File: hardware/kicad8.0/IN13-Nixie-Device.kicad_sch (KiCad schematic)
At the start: 35 parts, among them J1 PINHD_1x3_Female, J2 AudioJack3, J3 PINHD_1x4_Male, J4 USB_C_Receptacle_USB2.0_16P, Q2 MMBTA42, T1 Transformer_1P_1S, U1 LM358, U2 STI3508, U3 LD1117S33TR_SOT223, U4 ESP32-C6-MINI-1/U

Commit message: layout progress, kicad proj rename
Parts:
- removed C1: 1uF 16V, Capacitor_SMD:C_0805_2012Metric, symbol PCM_SL_Devices:Capacitor_NP
- removed C2: 10uF 16V, Capacitor_SMD:C_0805_2012Metric, symbol PCM_SL_Devices:Capacitor_NP
- removed D2: D_Schottky, Diode_SMD:D_0805_2012Metric, symbol Device:D_Schottky
- removed U3: LD1117S33TR_SOT223, Package_TO_SOT_THT:TO-220-3_Horizontal_TabDown, symbol Regulator_Linear:LD1117S33TR_SOT223
- added U3: AMS1117-3.3, Package_TO_SOT_SMD:SOT-223-3_TabPin2, symbol Regulator_Linear:AMS1117-3.3
- C10, C11: footprint Capacitor_SMD:C_0805_2012Metric -> Capacitor_SMD:C_0603_1608Metric
- R3, R6, R7, R8: footprint Resistor_SMD:R_0805_2012Metric -> Resistor_SMD:R_0603_1608Metric
- T1: footprint IN13-Device:EE0504S -> IN13-Nixie-Device:EE0504S; symbol IN13-Device:EE0504S_Transformer -> IN13-Nixie-Device:EE0504S_Transformer
- U2: symbol IN13-Device:STI3508 -> IN13-Nixie-Device:STI3508
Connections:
- net +3.3V: no longer T1.4 (AA), U2.5 (VIN)
- net +3V3: now also T1.4 (AA), U2.5 (VIN), U3.2 (VO)
- net GND: now also U3.1 (GND)
- net VBUS: now also C5.1, C6.1, U3.3 (VI)
- net VIN: no longer C5.1, C6.1
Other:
- note added: "Power/HV Boost"
- note removed: "Power"
- moved on the sheet: C3, C5, C6, C7, C8, C9, D1, J2, J3, J4, R1, R10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

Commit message: starting traces
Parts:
- added J5: PINHD_1x4_Male, SharedCustom:Pads_1x4_2.54mm, symbol PCM_SL_Pin_Headers:PINHD_1x4_Male
- added R11: 10k, Resistor_SMD:R_0603_1608Metric, symbol Device:R
- added SW1, SW3: SW_Push, IN13-Nixie-Device:Mitsumi_SOFSeries_SMD_Button, symbol IN13-Nixie-Device:SW_SPST_W_Ground_Pin
- C3: value 220nF 200V -> 0.22u 200V
- J3: footprint Connector_PinHeader_2.54mm:PinHeader_1x04_P2.54mm_Vertical -> SharedCustom:Pads_1x4_2.54mm
- U1: footprint Package_SO:SOIC-8-1EP_3.9x4.9mm_P1.27mm_EP2.41x3.81mm -> Package_SO:SOIC-8_3.9x4.9mm_P1.27mm
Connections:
- net +3V3 is gone; now on net +3.3V: C7.1, C8.1, C9.1, T1.4 (AA), U2.5 (VIN), U3.2 (VO)
- net +3.3V: now also R11.1
- net BOOT: now also SW3.1 (A)
- net GND: now also SW1.2 (B), SW1.3 (GND), SW3.2 (B), SW3.3 (GND)
- net SIGNAL: now also R11.2
- net TDI: now reaches U4.10 (MTDI/GPIO5/ADC1_CH5)
- net TDI: now also J5.2
- net TCK: now reaches U4.15 (MTCK/GPIO6/ADC1_CH6)
- net TCK: now also J5.3
- net TDO: now reaches U4.16 (MTDO/GPIO7)
- net TDO: now also J5.4
- net EN: now reaches C10.1, R6.2, U4.8 (EN/CHIP_PU)
- net EN: now also SW1.1 (A)
- net TMS: now reaches U4.9 (MTMS/GPIO4/ADC1_CH4)
- net TMS: now also J5.1
- no-connect marks 18 -> 14
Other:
- note added: "HV Boost"
- note added: "Power"
- note removed: "Power/HV Boost"
- title: IN-13 Device -> IN-13 Nixie Device
- moved on the sheet: C10, C11, C3, C5, C6, C7, C8, C9, D1, J2, J3, J4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

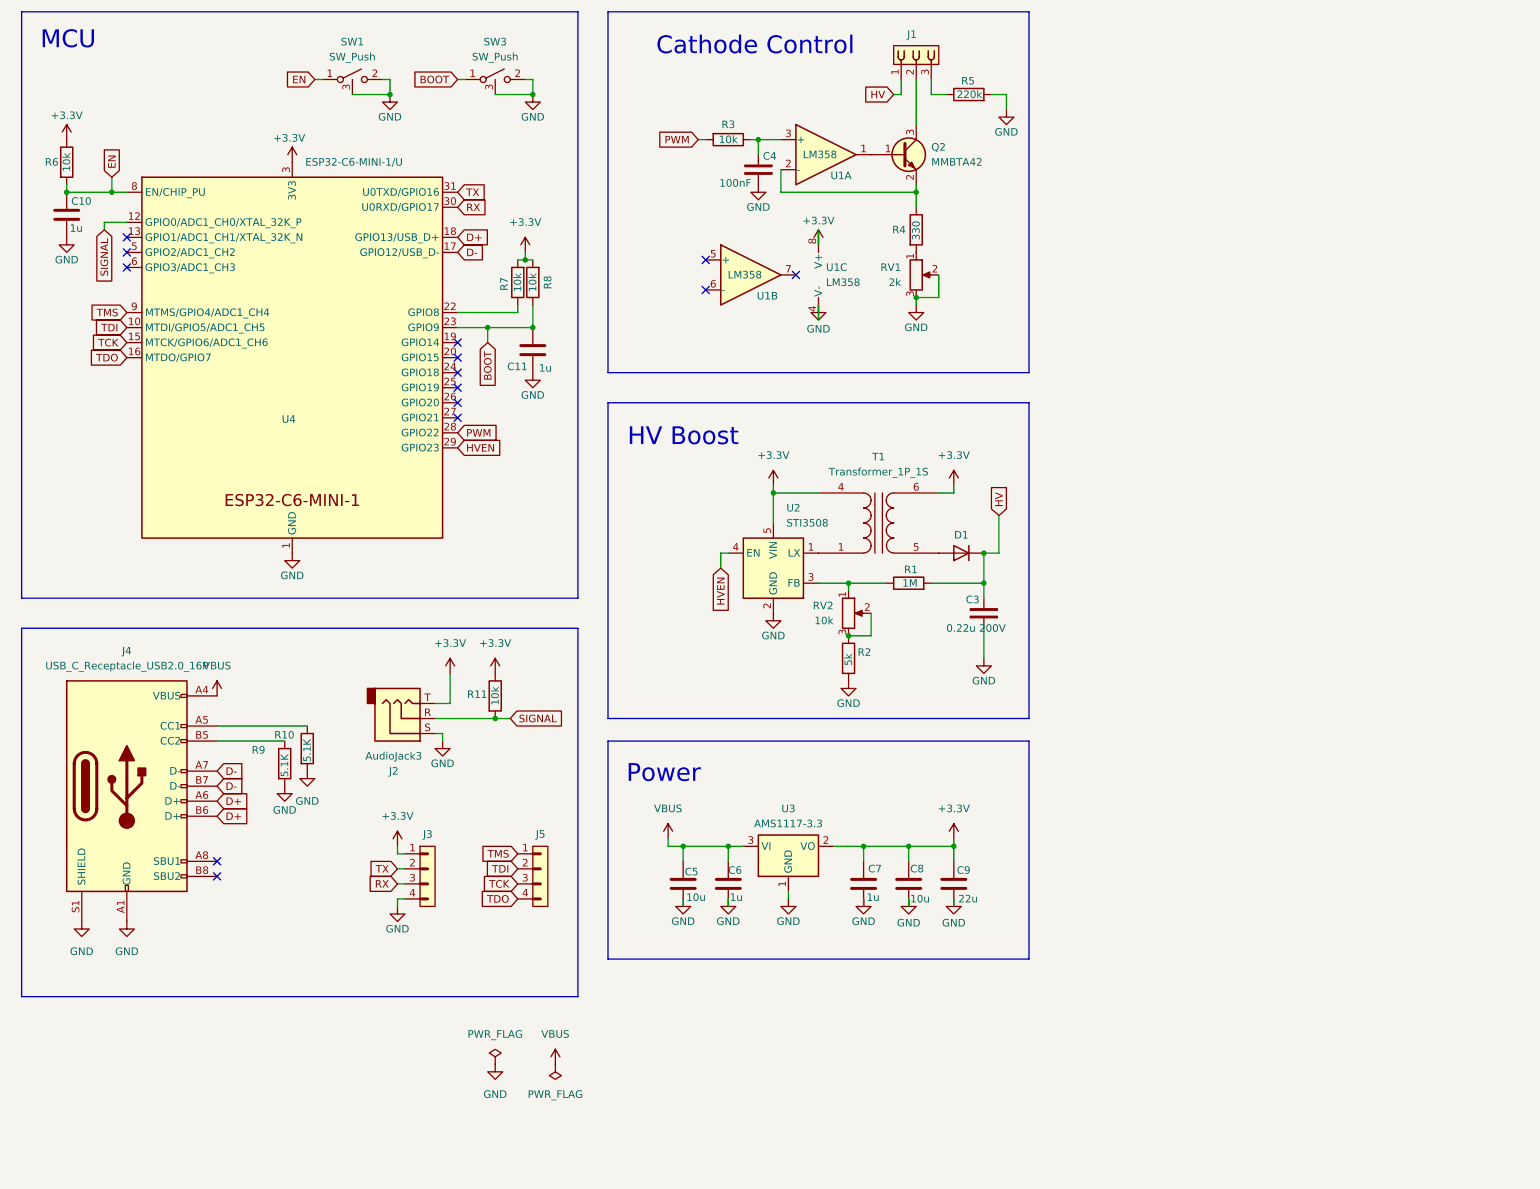
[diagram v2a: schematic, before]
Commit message: layout passing DRC (except USB conn)
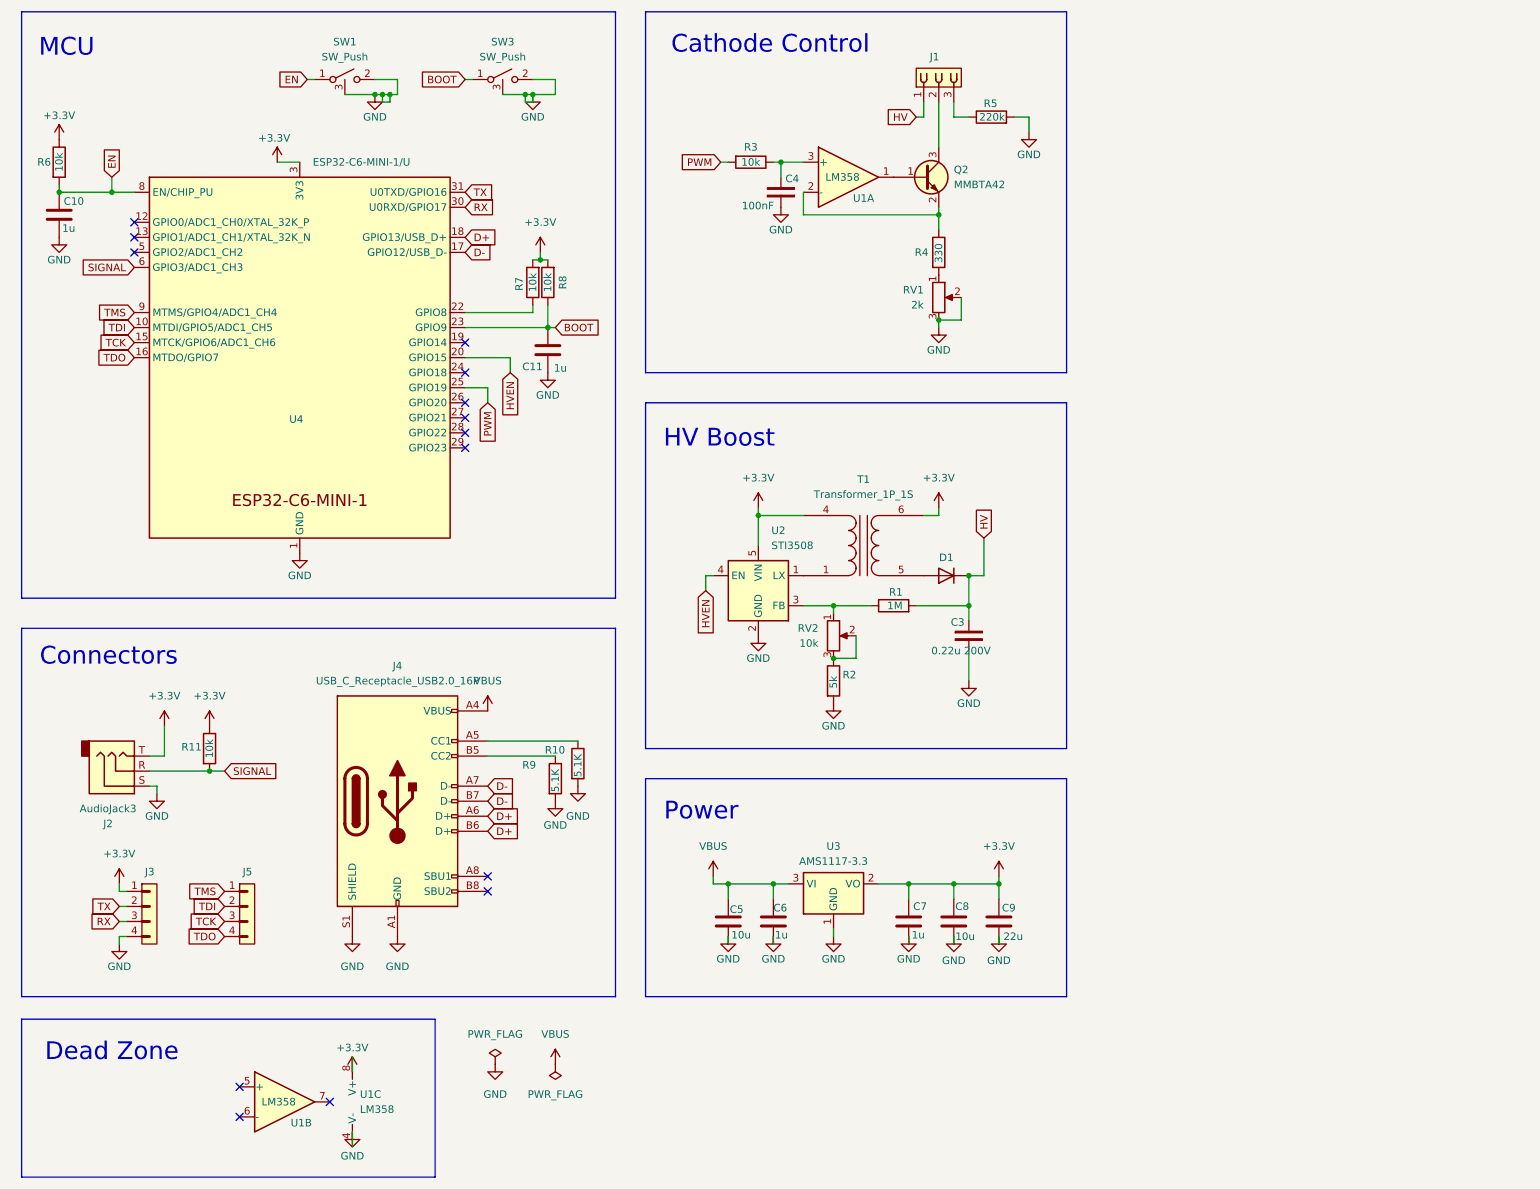
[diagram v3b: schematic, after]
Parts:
- J2: footprint Connector_Audio:Jack_3.5mm_CUI_SJ1-3523N_Horizontal -> IN13-Nixie-Device:Jack_3.5mm_CUI_SJ1-3523N_Horizontal_NoEdgeSilkscreen
- SW1, SW3: footprint IN13-Nixie-Device:Mitsumi_SOFSeries_SMD_Button -> IN13-Nixie-Device:Mitsumi_SOFSeries_SMD_Button_NoHoles
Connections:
- net HVEN: now also U4.20 (GPIO15); no longer U4.29 (GPIO23)
- net PWM: now also U4.25 (GPIO19); no longer U4.28 (GPIO22)
- net SIGNAL: now also U4.6 (GPIO3/ADC1_CH3); no longer U4.12 (GPIO0/ADC1_CH0/XTAL_32K_P)
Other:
- note added: "Connectors"
- note added: "Dead Zone"
- moved on the sheet: C10, C11, C3, C4, C5, C6, C7, C8, C9, D1, J1, J2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

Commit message: usb line adjust
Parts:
- added C1: 1u, Capacitor_SMD:C_0603_1608Metric, symbol Device:C
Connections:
- net +3.3V: now also C1.1
- net GND: now also C1.2
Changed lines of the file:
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@@
 	(wire
 		(pts
+			(xy 63.5 35.56) (xy 63.5 41.91)
+		)
+		(stroke
+			(width 0)
+			(type default)
+		)
+	)
+	(wire
+		(pts
 			(xy 153.67 116.84) (xy 160.02 116.84)
 		)
@@
 	(wire
 		(pts
-			(xy 63.5 41.91) (xy 59.69 41.91)
-		)
-		(stroke
-			(width 0)
-			(type default)
-		)
-	)
-	(wire
-		(pts
 			(xy 72.39 195.58) (xy 72.39 193.04)
 		)
@@
 	)
 	(symbol
+		(lib_id "power:+3.3V")
+		(at 45.72 26.67 0)
+		(unit 1)
+		(exclude_from_sim no)
+		(in_bom yes)
+		(on_board yes)
+		(dnp no)
+		(property "Reference" "#PWR040"
+			(at 45.72 30.48 0)
+			(effects
+				(font
+					(size 1.27 1.27)
+				)
+				(hide yes)
+			)
+		)
+		(property "Value" "+3.3V"
+			(at 45.212 22.606 0)
+			(effects
+				(font
+					(size 1.27 1.27)
+				)
+			)
+		)
+		(property "Footprint" ""
+			(at 45.72 26.67 0)
+			(effects
+				(font
+					(size 1.27 1.27)
+				)
+				(hide yes)
+			)
+		)
+		(property "Datasheet" ""
+			(at 45.72 26.67 0)
+			(effects
+				(font
+					(size 1.27 1.27)
+				)
+				(hide yes)
+			)
+		)
+		(property "Description" "Power symbol creates a global label with name \"+3.3V\""
+			(at 45.72 26.67 0)
+			(effects
+				(font
+					(size 1.27 1.27)
+				)
+				(hide yes)
+			)
+		)
+		(pin "1"
+		)
+		(instances
+			(project "IN13-Nixie-Device"
+				(path "/36cde5b7-6663-4cfe-a0a3-3f17918aab11"
+					(reference "#PWR040")
+					(unit 1)
+				)
+			)
+		)
+	)
+	(symbol
 		(lib_id "power:GND")
 		(at 80.01 172.72 0)
@@
 	(symbol
 		(lib_id "power:GND")
+		(at 45.72 34.29 0)
+		(unit 1)
+		(exclude_from_sim no)
+		(in_bom yes)
+		(on_board yes)
+		(dnp no)
+		(property "Reference" "#PWR039"
+			(at 45.72 40.64 0)
+			(effects
+				(font
+					(size 1.27 1.27)
+				)
+				(hide yes)
+			)
+		)
+		(property "Value" "GND"
+			(at 45.72 38.1 0)
+			(effects
+				(font
+					(size 1.27 1.27)
+				)
+			)
+		)
+		(property "Footprint" ""
+			(at 45.72 34.29 0)
+			(effects
+				(font
+					(size 1.27 1.27)
+				)
+				(hide yes)
+			)
+		)
+		(property "Datasheet" ""
+			(at 45.72 34.29 0)
+			(effects
+				(font
+					(size 1.27 1.27)
+				)
+				(hide yes)
+			)
+		)
+		(property "Description" "Power symbol creates a global label with name \"GND\" , ground"
+			(at 45.72 34.29 0)
+			(effects
+				(font
+					(size 1.27 1.27)
+				)
+				(hide yes)
+			)
+		)
+		(pin "1"
+		)
+		(instances
+			(project "IN13-Nixie-Device"
+				(path "/36cde5b7-6663-4cfe-a0a3-3f17918aab11"
+					(reference "#PWR039")
+					(unit 1)
+				)
+			)
+		)
+	)
+	(symbol
+		(lib_id "power:GND")
 		(at 106.68 149.86 0)
 		(unit 1)
@@
 	(symbol
 		(lib_id "power:+3.3V")
-		(at 59.69 41.91 0)
+		(at 63.5 35.56 0)
 		(unit 1)
 		(exclude_from_sim no)
@@
 		(dnp no)
 		(property "Reference" "#PWR017"
-			(at 59.69 45.72 0)
+			(at 63.5 39.37 0)
 			(effects
 				(font
@@
 		)
 		(property "Value" "+3.3V"
-			(at 59.182 37.846 0)
+			(at 62.992 31.496 0)
 			(effects
 				(font
@@
 		)
 		(property "Footprint" ""
-			(at 59.69 41.91 0)
+			(at 63.5 35.56 0)
 			(effects
 				(font
@@
 		)
 		(property "Datasheet" ""
-			(at 59.69 41.91 0)
+			(at 63.5 35.56 0)
 			(effects
 				(font
@@
 		)
 		(property "Description" "Power symbol creates a global label with name \"+3.3V\""
-			(at 59.69 41.91 0)
+			(at 63.5 35.56 0)
 			(effects
 				(font
@@
 					(unit 1)
 				)
+			)
+		)
+	)
+	(symbol
+		(lib_id "Device:C")
+		(at 45.72 30.48 0)
+		(unit 1)
+		(exclude_from_sim no)
+		(in_bom yes)
+		(on_board yes)
+		(dnp no)
+		(property "Reference" "C1"
+			(at 46.482 27.94 0)
+			(effects
+				(font
+					(size 1.27 1.27)
+				)
+				(justify left)
+			)
+		)
+		(property "Value" "1u"
+			(at 46.228 32.766 0)
+			(effects
+				(font
+					(size 1.27 1.27)
+				)
+				(justify left)
+			)
+		)
+		(property "Footprint" "Capacitor_SMD:C_0603_1608Metric"
+			(at 46.6852 34.29 0)
+			(effects
+				(font
+					(size 1.27 1.27)
+				)
+				(hide yes)
+			)
+		)
+		(property "Datasheet" "~"
+			(at 45.72 30.48 0)
+			(effects
+				(font
+					(size 1.27 1.27)
+				)
+				(hide yes)
+			)
+		)
+		(property "Description" "Unpolarized capacitor"
+			(at 45.72 30.48 0)
+			(effects
+				(font
+					(size 1.27 1.27)
+				)
+				(hide yes)
+			)
+		)
+		(pin "1"
+		)
+		(pin "2"
+		)
+		(instances
+			(project "IN13-Nixie-Device"
+				(path "/36cde5b7-6663-4cfe-a0a3-3f17918aab11"
+					(reference "C1")
+					(unit 1)
+				)

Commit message: final board revisions and images
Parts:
- added TP1, TP2, TP3: TestPoint, TestPoint:TestPoint_Pad_1.0x1.0mm, symbol Connector:TestPoint
- SW1, SW3: footprint IN13-Nixie-Device:Mitsumi_SOFSeries_SMD_Button_NoHoles -> IN13-Nixie-Device:Mitsumi_SOFSeries_SMD_Button
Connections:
- net HV: now also TP3.1
- net HVEN: now also TP2.1
- net PWM: now also TP1.1
